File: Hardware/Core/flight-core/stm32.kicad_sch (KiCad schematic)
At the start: 13 parts, among them SW1 SW_SPDT, SW2 SW_MEC_5E, U1 STM32G473CCTx, Y1 48 MHZ

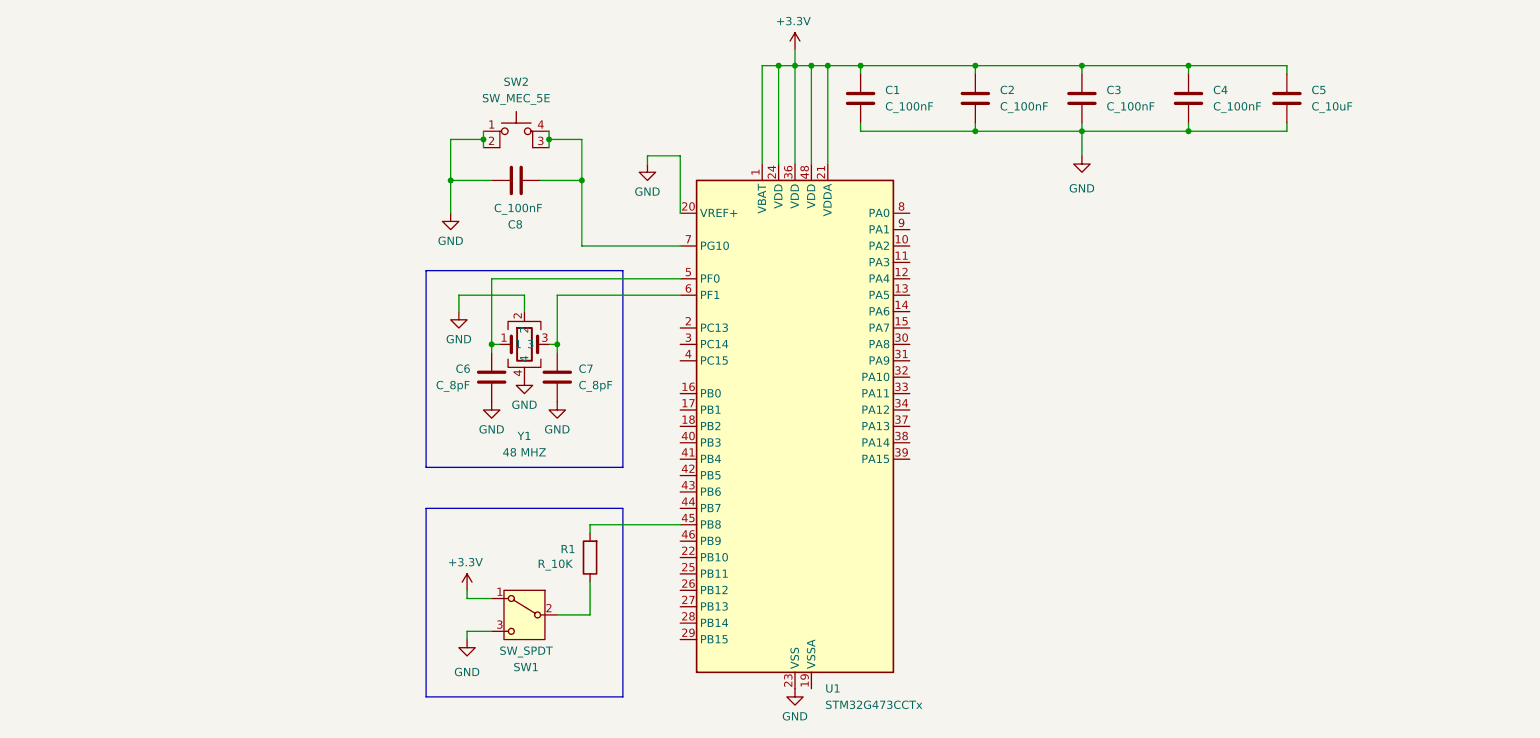
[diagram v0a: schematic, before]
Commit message: added df17 part to library, added stm32 actual names of pins
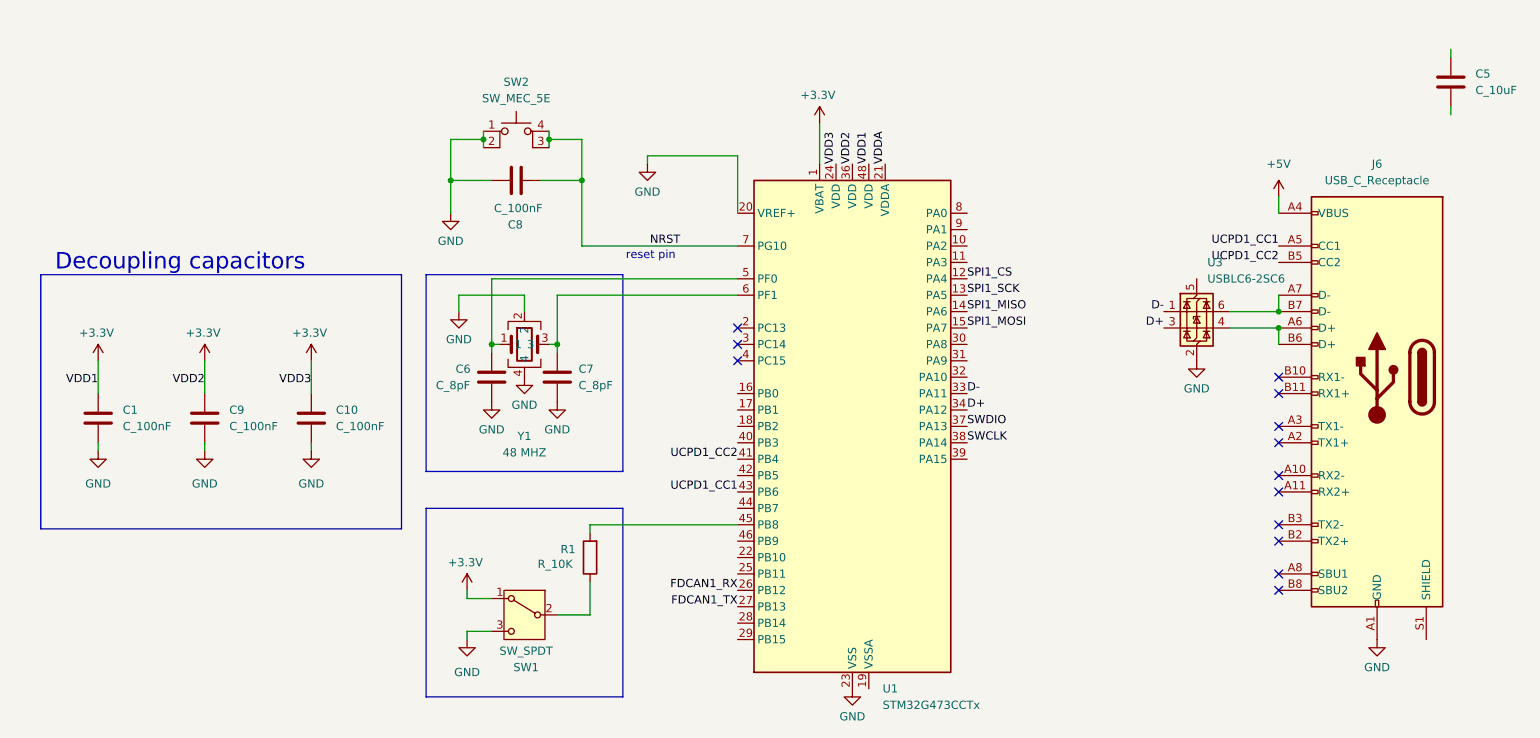
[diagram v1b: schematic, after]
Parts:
- removed C2, C3, C4: C_100nF, footprints:C_0603_1608Metric, symbol formula:C_100nF
- added C10, C9: C_100nF, footprints:C_0603_1608Metric, symbol formula:C_100nF
- added J6: USB_C_Receptacle, Connector_USB:USB_C_Receptacle_Molex_105450-0101, symbol Connector:USB_C_Receptacle
- added U3: USBLC6-2SC6, Package_TO_SOT_SMD:SOT-23-6, symbol Power_Protection:USBLC6-2SC6
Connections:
- net +3.3V: now also C10.1, C9.1; no longer C5.1, U1.21 (VDDA)
- net GND: now also C10.2, C9.2, J6.A1 (GND), J6.A12 (GND), J6.B1 (GND), J6.B12 (GND), U3.2 (GND); no longer C5.2
- net SPI1_CS: now reaches U1.12 (PA4)
- net SPI1_SCK: now reaches U1.13 (PA5)
- net SPI1_MISO: now reaches U1.14 (PA6)
- net SPI1_MOSI: now reaches U1.15 (PA7)
- net FDCAN1_RX: now reaches U1.26 (PB12)
- net FDCAN1_TX: now reaches U1.27 (PB13)
- net D-: now reaches U1.33 (PA11)
- net D-: now also U3.1 (I/O1)
- net D+: now reaches U1.34 (PA12)
- net D+: now also U3.3 (I/O2)
- net SWDIO: now reaches U1.37 (PA13)
- net SWCLK: now reaches U1.38 (PA14)
- net UCPD1_CC2: now reaches U1.41 (PB4)
- net UCPD1_CC2: now also J6.B5 (CC2)
- net UCPD1_CC1: now reaches U1.43 (PB6)
- net UCPD1_CC1: now also J6.A5 (CC1)
- net NRST: now reaches C8.2, SW2.3 (K), SW2.4 (A), U1.7 (PG10)
- new net: J6.A6 (D+), J6.B6 (D+), U3.4 (I/O2)
- new net: J6.A7 (D-), J6.B7 (D-), U3.6 (I/O1)
- new net +5V: J6.A4 (VBUS), J6.A9 (VBUS), J6.B4 (VBUS), J6.B9 (VBUS)
- new net VDDA: U1.21 (VDDA)
- no-connect marks 0 -> 13
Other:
- note added: "Decoupling capacitors"
- note added: "reset pin"
- moved on the sheet: C1, C5, U1

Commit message: adding cube connector
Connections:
- net +5V: now also U3.5 (VBUS)
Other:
- moved on the sheet: U3
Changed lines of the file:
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@@
 	(wire
 		(pts
-			(xy 203.2 86.36) (xy 210.82 86.36)
+			(xy 198.12 86.36) (xy 210.82 86.36)
 		)
 		(stroke
@@
 	(wire
 		(pts
-			(xy 203.2 88.9) (xy 210.82 88.9)
+			(xy 198.12 88.9) (xy 210.82 88.9)
 		)
 		(stroke
@@
 	)
 	(label "D+"
-		(at 193.04 88.9 180)
+		(at 187.96 88.9 180)
 		(effects
 			(font
@@
 	)
 	(label "D-"
-		(at 193.04 86.36 180)
+		(at 187.96 86.36 180)
 		(effects
 			(font
@@
 	(symbol
 		(lib_id "power:GND")
-		(at 198.12 93.98 0)
+		(at 193.04 93.98 0)
 		(unit 1)
 		(exclude_from_sim no)
@@
 		(dnp no)
 		(property "Reference" "#PWR025"
-			(at 198.12 100.33 0)
+			(at 193.04 100.33 0)
 			(effects
 				(font
@@
 		)
 		(property "Value" "GND"
-			(at 198.12 98.298 0)
+			(at 193.04 98.298 0)
 			(effects
 				(font
@@
 		)
 		(property "Footprint" ""
-			(at 198.12 93.98 0)
+			(at 193.04 93.98 0)
 			(effects
 				(font
@@
 		)
 		(property "Datasheet" ""
-			(at 198.12 93.98 0)
+			(at 193.04 93.98 0)
 			(effects
 				(font
@@
 		)
 		(property "Description" "Power symbol creates a global label with name \"GND\" , ground"
-			(at 198.12 93.98 0)
+			(at 193.04 93.98 0)
 			(effects
 				(font
@@
 	(symbol
 		(lib_id "Power_Protection:USBLC6-2SC6")
-		(at 198.12 86.36 0)
+		(at 193.04 86.36 0)
 		(unit 1)
 		(exclude_from_sim no)
@@
 		(fields_autoplaced yes)
 		(property "Reference" "U3"
-			(at 199.7711 78.74 0)
+			(at 194.6911 78.74 0)
 			(effects
 				(font
@@
 		)
 		(property "Value" "USBLC6-2SC6"
-			(at 199.7711 81.28 0)
+			(at 194.6911 81.28 0)
 			(effects
 				(font
@@
 		)
 		(property "Footprint" "Package_TO_SOT_SMD:SOT-23-6"
-			(at 199.39 92.71 0)
+			(at 194.31 92.71 0)
 			(effects
 				(font
@@
 		)
 		(property "Datasheet" "https://www.st.com/resource/en/datasheet/usblc6-2.pdf"
-			(at 199.39 94.615 0)
+			(at 194.31 94.615 0)
 			(effects
 				(font
@@
 		)
 		(property "Description" "Very low capacitance ESD protection diode, 2 data-line, SOT-23-6"
-			(at 198.12 86.36 0)
+			(at 193.04 86.36 0)
 			(effects
 				(font
@@
 					(unit 1)
 				)
+			)
+		)
+	)
+	(symbol
+		(lib_id "power:+5V")
+		(at 193.04 81.28 0)
+		(unit 1)
+		(exclude_from_sim no)
+		(in_bom yes)
+		(on_board yes)
+		(dnp no)
+		(fields_autoplaced yes)
+		(property "Reference" "#PWR028"
+			(at 193.04 85.09 0)
+			(effects
+				(font
+					(size 1.27 1.27)
+				)
+				(hide yes)
+			)
+		)
+		(property "Value" "+5V"
+			(at 193.04 76.2 0)
+			(effects
+				(font
+					(size 1.27 1.27)
+				)
+			)
+		)
+		(property "Footprint" ""
+			(at 193.04 81.28 0)
+			(effects
+				(font
+					(size 1.27 1.27)
+				)
+				(hide yes)
+			)
+		)
+		(property "Datasheet" ""
+			(at 193.04 81.28 0)
+			(effects
+				(font
+					(size 1.27 1.27)
+				)
+				(hide yes)
+			)
+		)
+		(property "Description" "Power symbol creates a global label with name \"+5V\""
+			(at 193.04 81.28 0)
+			(effects
+				(font
+					(size 1.27 1.27)
+				)
+				(hide yes)
+			)
+		)
+		(pin "1"
+		)
+		(instances
+			(project "flight-core"
+				(path "/93f46f4b-cdf5-47ec-af03-96378e73b2e1/91e18f07-bd3f-4576-bbe1-a0227cf7132e"
+					(reference "#PWR028")
+					(unit 1)
+				)
